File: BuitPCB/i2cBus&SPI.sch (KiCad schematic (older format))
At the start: 18 parts, among them J10 Conn_01x06, J11 Conn_01x04, J12 Conn_01x04, J13 Conn_01x04, J14 Conn_01x04, J15 Conn_01x04, J16 Conn_01x04, J17 Conn_01x04, J18 Conn_01x04, J7 Conn_01x06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

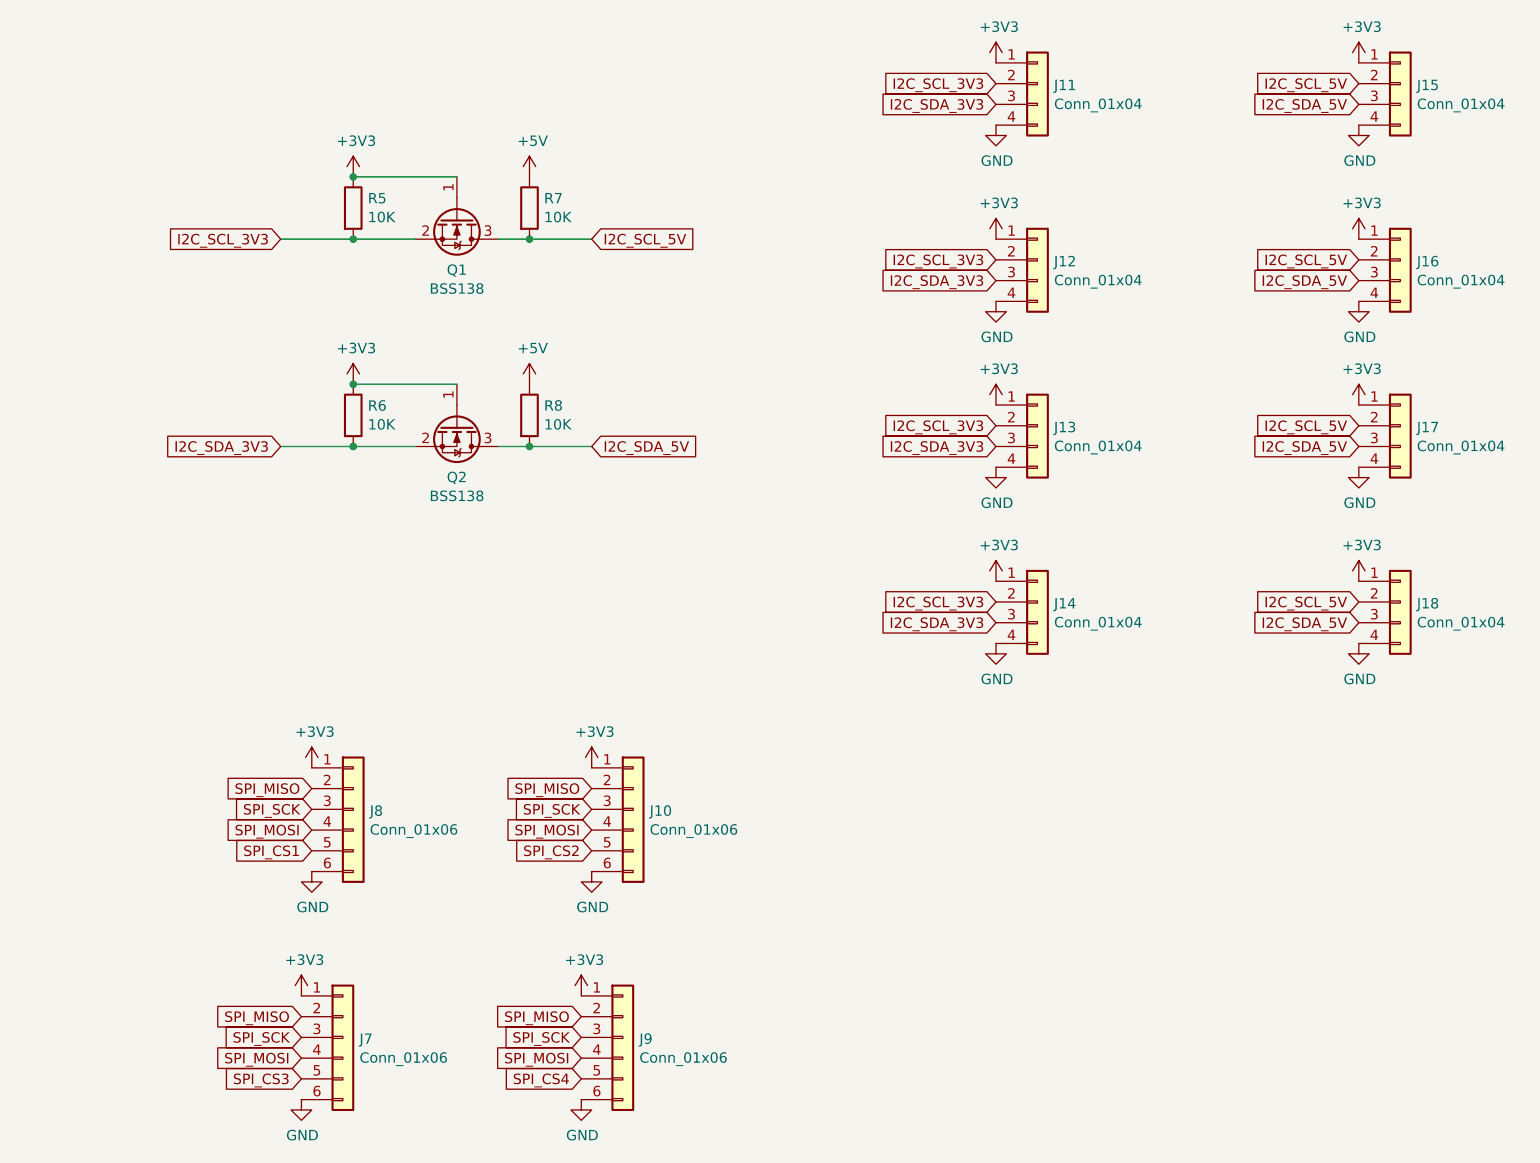
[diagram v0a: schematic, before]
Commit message: Added sensors connectors
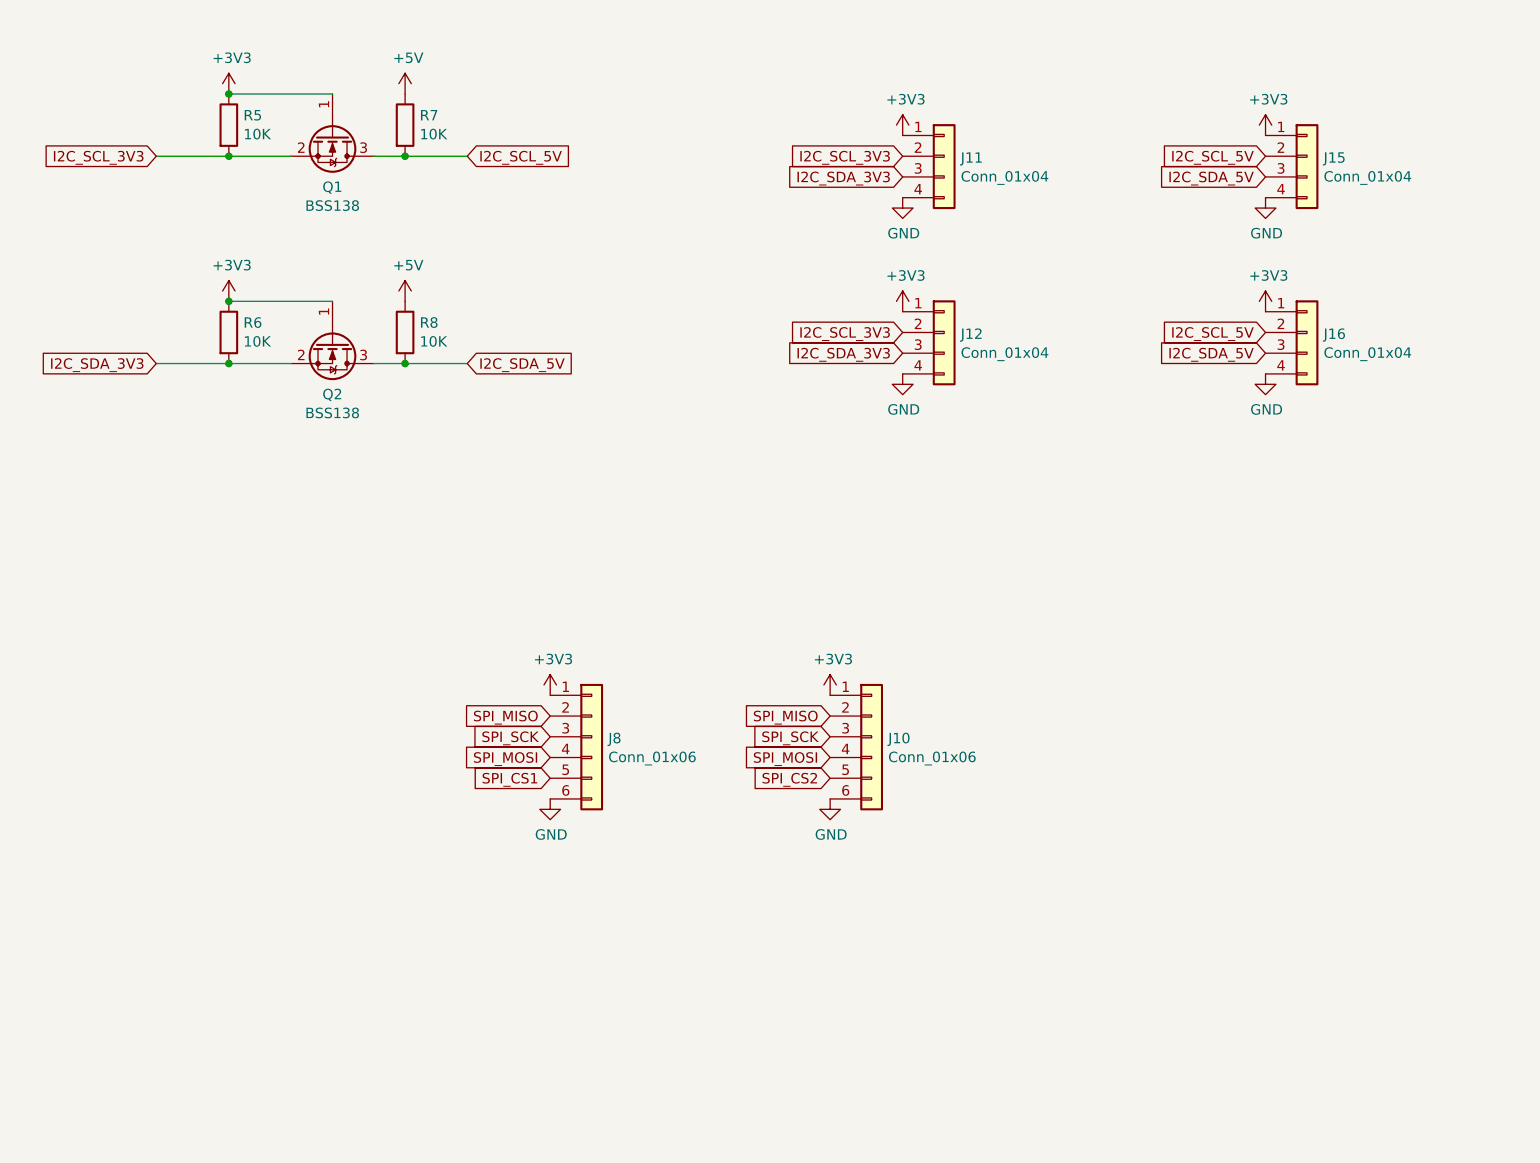
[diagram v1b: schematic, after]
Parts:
- removed J13, J14, J17, J18: Conn_01x04, Connector_JST:JST_XH_B4B-XH-A_1x04_P2.50mm_Vertical, symbol Connector_Generic:Conn_01x04
- removed J7, J9: Conn_01x06, Connector_JST:JST_XH_B6B-XH-A_1x06_P2.50mm_Vertical, symbol Connector_Generic:Conn_01x06
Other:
- moved on the sheet: J10, J11, J12, J15, J16, J8, Q1, Q2, R5, R6, R7, R8

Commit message: Updated to almost every component and started routing
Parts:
- removed J10, J8: Conn_01x06, Connector_JST:JST_XH_B6B-XH-A_1x06_P2.50mm_Vertical, symbol Connector_Generic:Conn_01x06
- J11: value Conn_01x04 -> OLED DISPLAY
- J12: value Conn_01x04 -> NEO TRELLIS
- J15, J16: value Conn_01x04 -> I2C DEV 5V
